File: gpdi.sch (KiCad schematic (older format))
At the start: 13 parts, among them U1 LFE5U-85F-6BG381C

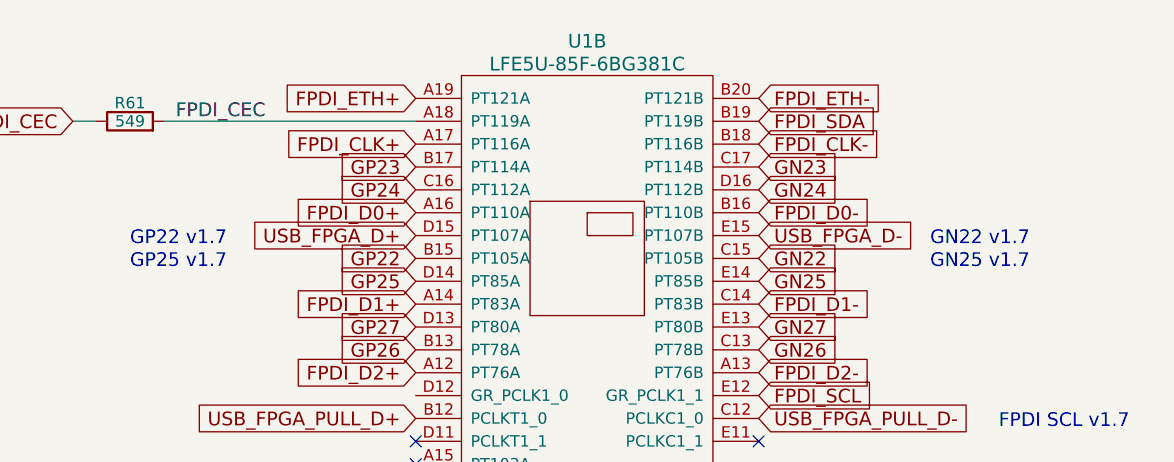
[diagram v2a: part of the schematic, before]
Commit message: Adding SPI from FPGA
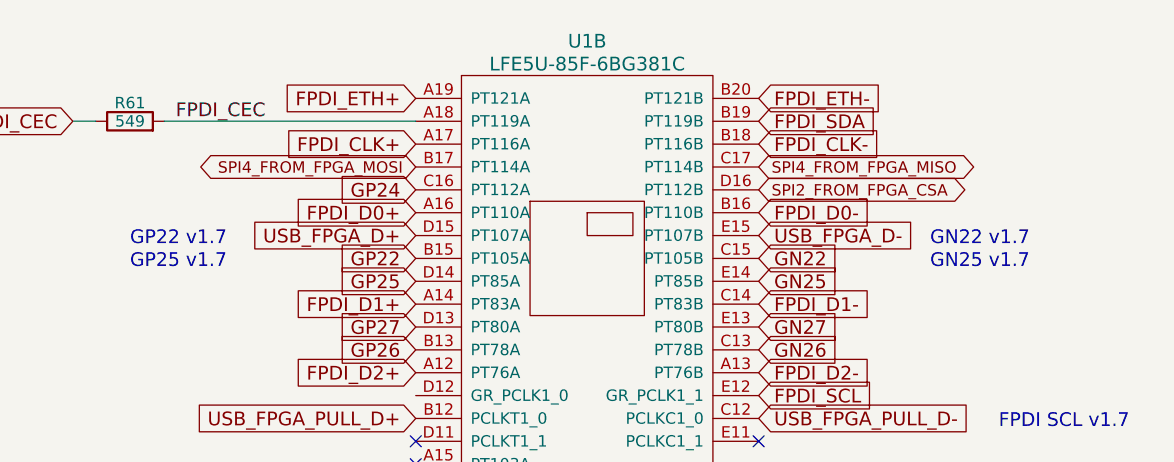
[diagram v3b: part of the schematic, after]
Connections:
- net GN23 renamed SPI4_FROM_FPGA_MISO
- net GN24 renamed SPI2_FROM_FPGA_CSA
- net GP23 renamed SPI4_FROM_FPGA_MOSI
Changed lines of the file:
@@
 Text GLabel 4350 2900 2    60   Input ~ 0
 GN22
-Text GLabel 4350 2500 2    60   Input ~ 0
-GN23
-Text GLabel 4350 2600 2    60   Input ~ 0
-GN24
 Text GLabel 4350 3000 2    60   Input ~ 0
 GN25
@@
 Text GLabel 2850 2600 0    60   Input ~ 0
 GP24
-Text GLabel 2850 2500 0    60   Input ~ 0
-GP23
 Text GLabel 2850 3300 0    60   Input ~ 0
 GP26
@@
 NoConn ~ 2850 3800
 NoConn ~ 4350 3700
+Text GLabel 4350 2500 2    50   BiDi ~ 0
+SPI4_FROM_FPGA_MISO
+Text GLabel 2850 2500 0    50   BiDi ~ 0
+SPI4_FROM_FPGA_MOSI
+Text GLabel 4350 2600 2    50   BiDi ~ 0
+SPI2_FROM_FPGA_CSA
 $EndSCHEMATC
